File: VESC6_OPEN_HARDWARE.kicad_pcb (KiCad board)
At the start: 2 copper layers, 112.6 x 46.7 mm, 124 parts, among them P1 USB_OTG, P10 PH_A, P11 SUPPLY, P12 GND, P2 TS_CAN, P3 SWD, P4 HALL/Encoder, P7 Custom, P8 PH_C, P9 PH_B, Q1 STL130N6F7, Q2 STL130N6F7, Q3 STL130N6F7, Q4 STL130N6F7, Q5 STL130N6F7, Q6 STL130N6F7, U1 STM32F40X_LQFP64, U10 LSM6DS3TR-C, U2 LM3671, U3 DRV8301, U4 TJA1051TK-3, U5 AD8418, U6 AD8418, U7 AD8418, X1 8m

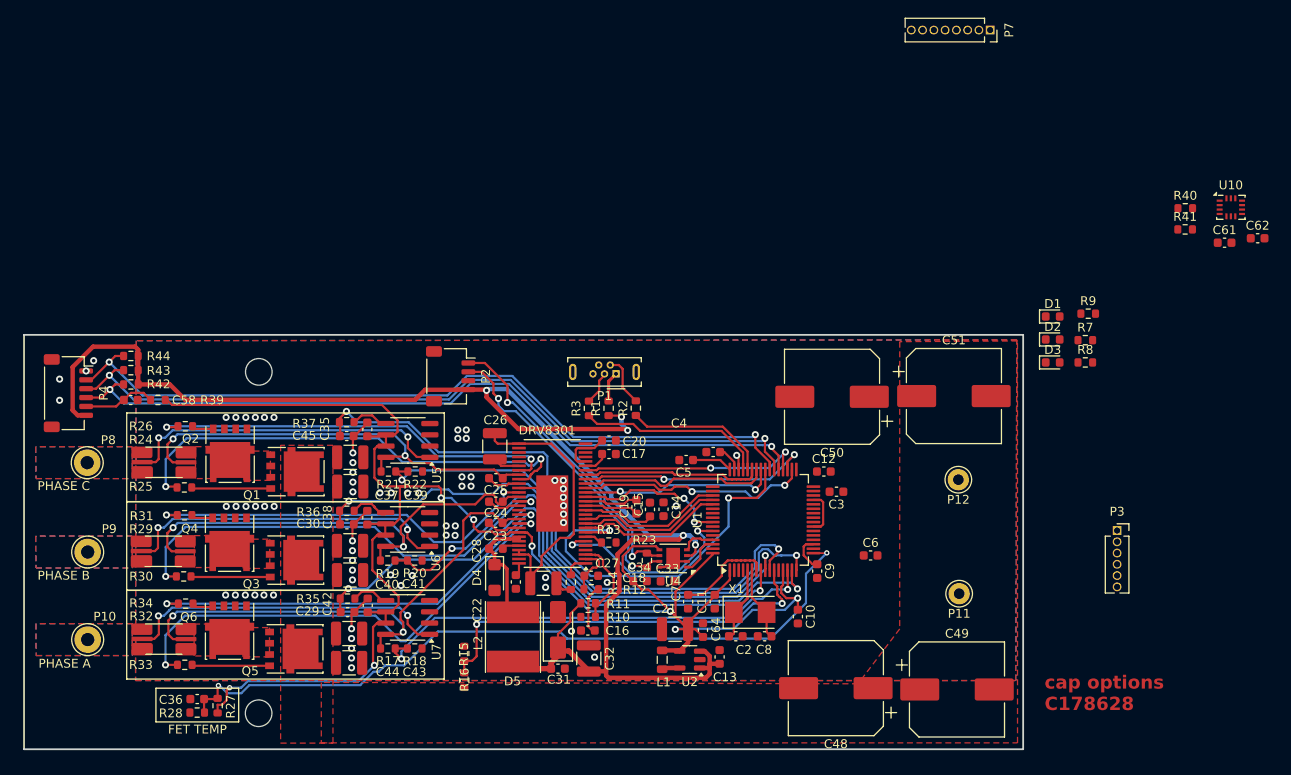
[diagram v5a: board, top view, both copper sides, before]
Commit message: More routing, positioning and SMT USB
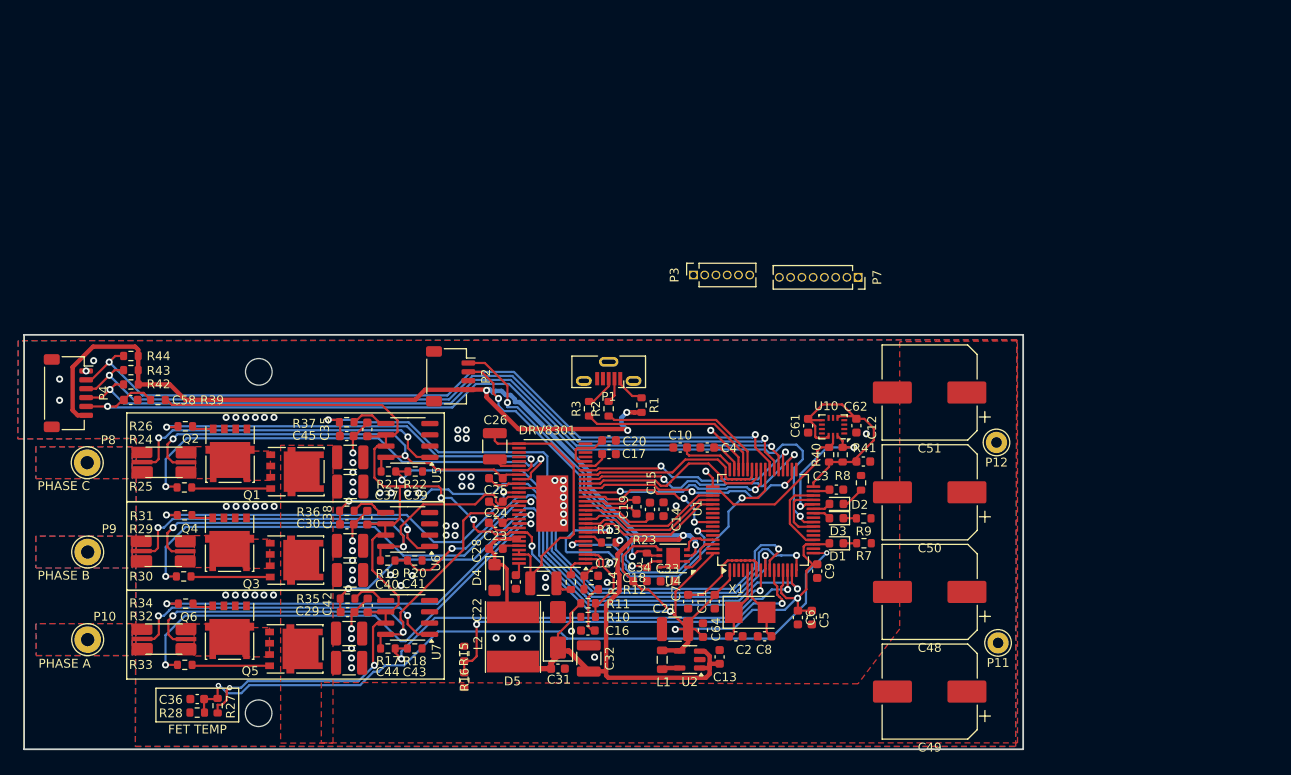
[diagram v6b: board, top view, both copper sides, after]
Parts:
- C48, C49, C50, C51: value 680u_63v -> 220u_63v
- P1: footprint Connector_USB:USB_Micro-B_Wuerth_614105150721_Vertical -> Connector_USB:USB_Micro-B_Molex-105133-0001
- moved P3 55.8 mm to (106.3, 21.2), turned to 90 degrees
- moved C61 51.3 mm to (119.2, 38.2), turned to 90 degrees
- moved U10 51.2 mm to (122.0, 38.3), turned to 180 degrees
- moved C62 49.9 mm to (124.6, 38.2), turned to 90 degrees
- moved R40 48.8 mm to (121.6, 41.5), turned to 90 degrees
- moved R41 46.2 mm to (123.1, 41.5), turned to -90 degrees
- moved D1 35.3 mm to (122.4, 51.4), turned to 180 degrees
- moved R9 34.3 mm to (125.5, 48.6)
- moved R7 33.9 mm to (125.5, 51.4), turned to 180 degrees
- moved P7 31.6 mm to (124.8, 21.5)
- moved D2 30.6 mm to (122.4, 47.0), turned to 180 degrees
- moved D3 30.1 mm to (122.4, 48.6), turned to 180 degrees
- moved R8 28.7 mm to (125.2, 44.6), turned to 90 degrees
- moved C10 23.2 mm to (104.8, 40.6), turned to 180 degrees
- moved C5 22.7 mm to (119.6, 59.8), turned to -90 degrees
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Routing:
- net /stm32f40x/TEMP_MOTOR: track 8.37 -> 102.0 mm, vias 0 -> 2
- net VCC: track 206.3 -> 244.7 mm
- net /IMU/SCL: track 0.00 -> 18.6 mm
- net /IMU/SDA: track 0.00 -> 15.3 mm, vias 0 -> 2
- net /stm32f40x/RX_SDA_NSS: track 0.00 -> 9.16 mm
- net /stm32f40x/SWDIO: track 1.69 -> 5.78 mm
- net /stm32f40x/USB_DM: track 16.3 -> 19.4 mm
- net Net-(P1-D-): track 5.80 -> 2.84 mm
- net Net-(D2-K): track 0.00 -> 2.63 mm
- net /stm32f40x/TX_SCL_MOSI: track 4.90 -> 7.23 mm
- net /stm32f40x/SWCLK: track 0.00 -> 2.06 mm, vias 0 -> 1
- net /stm32f40x/LED_RED: track 0.00 -> 2.04 mm
- net /stm32f40x/LED_GREEN: track 0.00 -> 2.03 mm
- net Net-(U1-VCAP1): track 0.00 -> 1.88 mm
- net +5V: track 174.7 -> 176.6 mm
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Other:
- board text added: "ADC port Aditional CAN port for BMS"
- board text removed: "Mounting hole placement SMD electrolytic Cap placement Phase and power connector sizes"
- board text removed: "cap options C178628"

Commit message: Routing cleanup
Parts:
- moved L2 1.06 mm to (84.9, 62.0)
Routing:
- net VCC: track 244.7 -> 270.5 mm, vias 8 -> 10
- net SUPPLY: track 30.9 -> 43.1 mm, vias 0 -> 2
- net /DRV8301/SENS_SUPPLY: track 46.1 -> 47.8 mm
- net Net-(U3-GVDD): track 8.07 -> 9.61 mm
- net /DRV8301/INH_B: track 23.0 -> 23.5 mm
- net GND: vias 75 -> 85

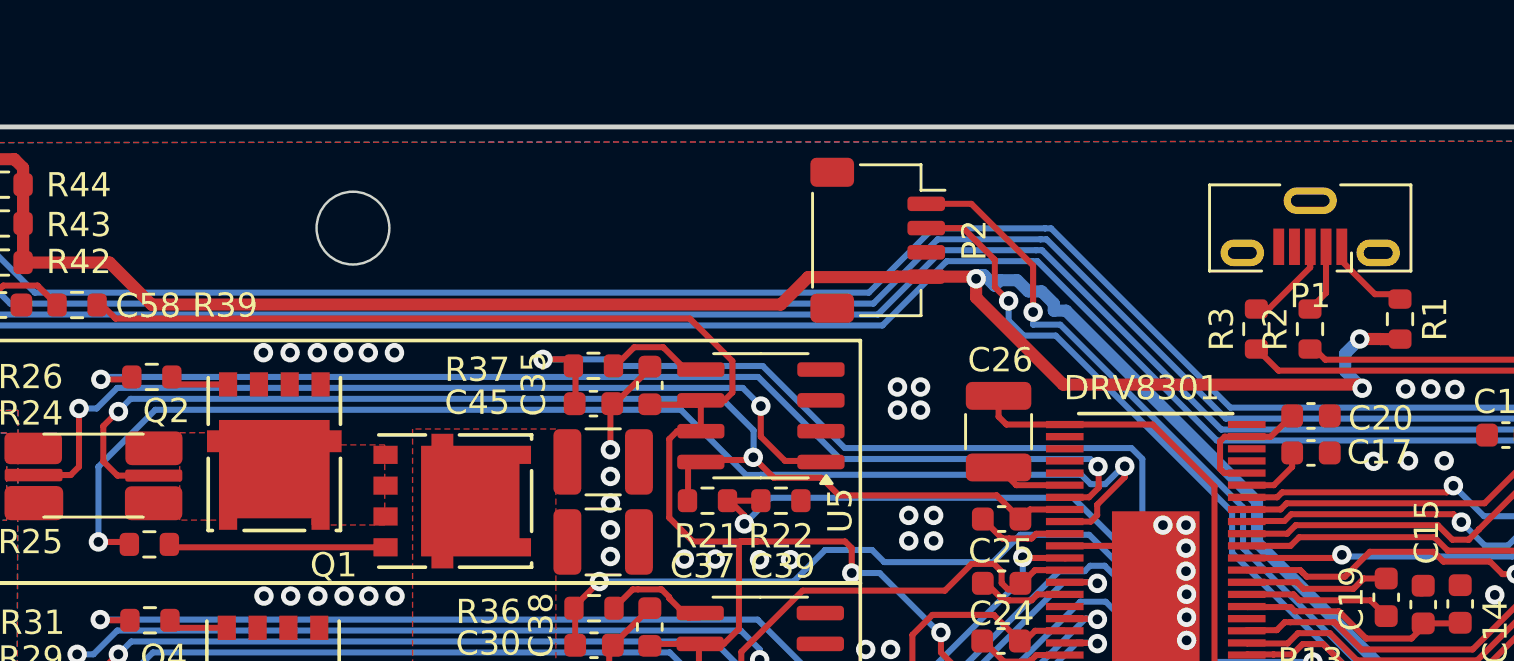
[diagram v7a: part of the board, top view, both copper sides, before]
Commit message: double CAN ports
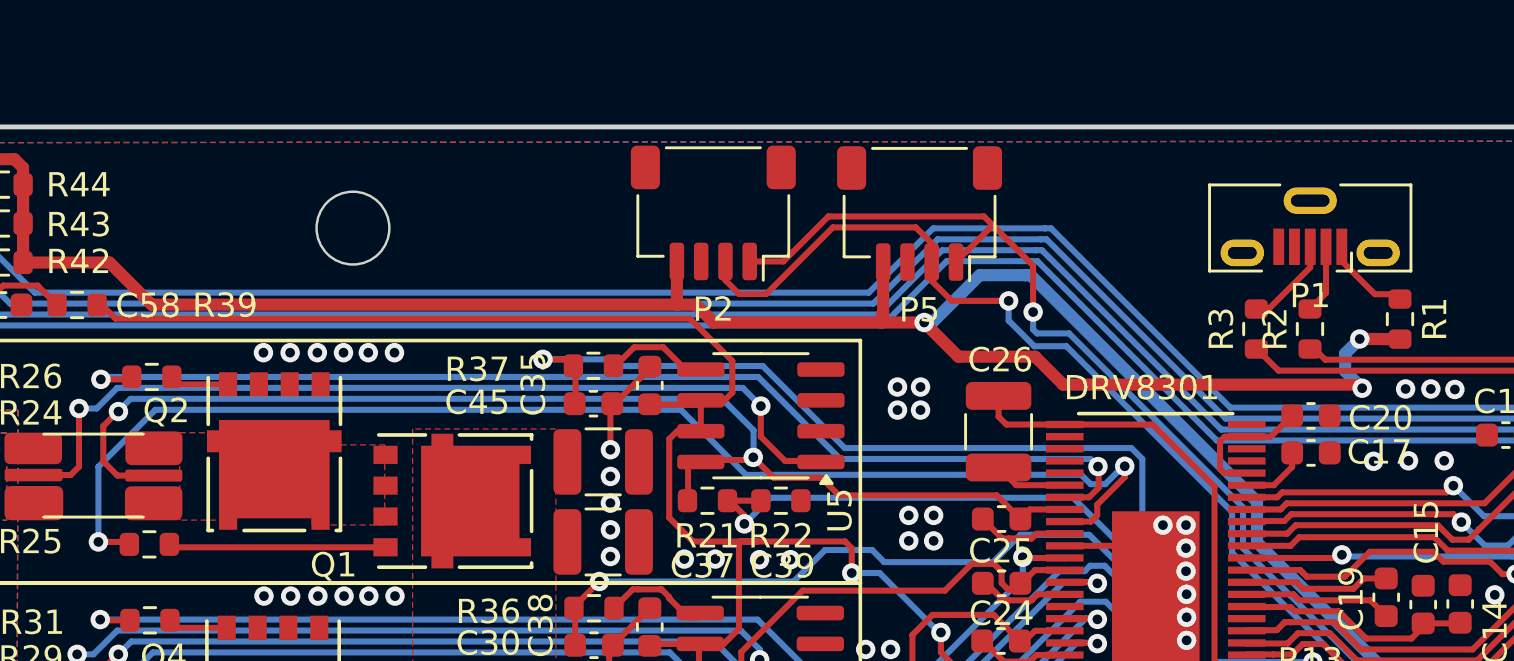
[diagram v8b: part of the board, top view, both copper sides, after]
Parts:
- added P5: TS_CAN, Connector_JST:JST_SH_SM04B-SRSS-TB_1x04-1MP_P1.00mm_Horizontal, F.Cu at (80.6, 31.5)
- moved P2 6.87 mm to (72.1, 31.5), turned to 180 degrees
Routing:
- net /CAN/CANH: track 34.1 -> 45.4 mm
- net /CAN/CANL: track 34.1 -> 44.8 mm
- net +5V: track 176.6 -> 182.0 mm
